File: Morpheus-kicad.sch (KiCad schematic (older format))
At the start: 60 parts, among them J1 Conn_02x03_Odd_Even, J2 Conn_02x03_Odd_Even, J3 Conn_02x03_Odd_Even, J4 Conn_02x03_Odd_Even, J5 Conn_02x05_Counter_Clockwise, J6 Conn_01x05, Q1 IRLZ44N, Q2 IRLB3034PBF, Q3 IRLZ44N, U1 Pololu Driver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

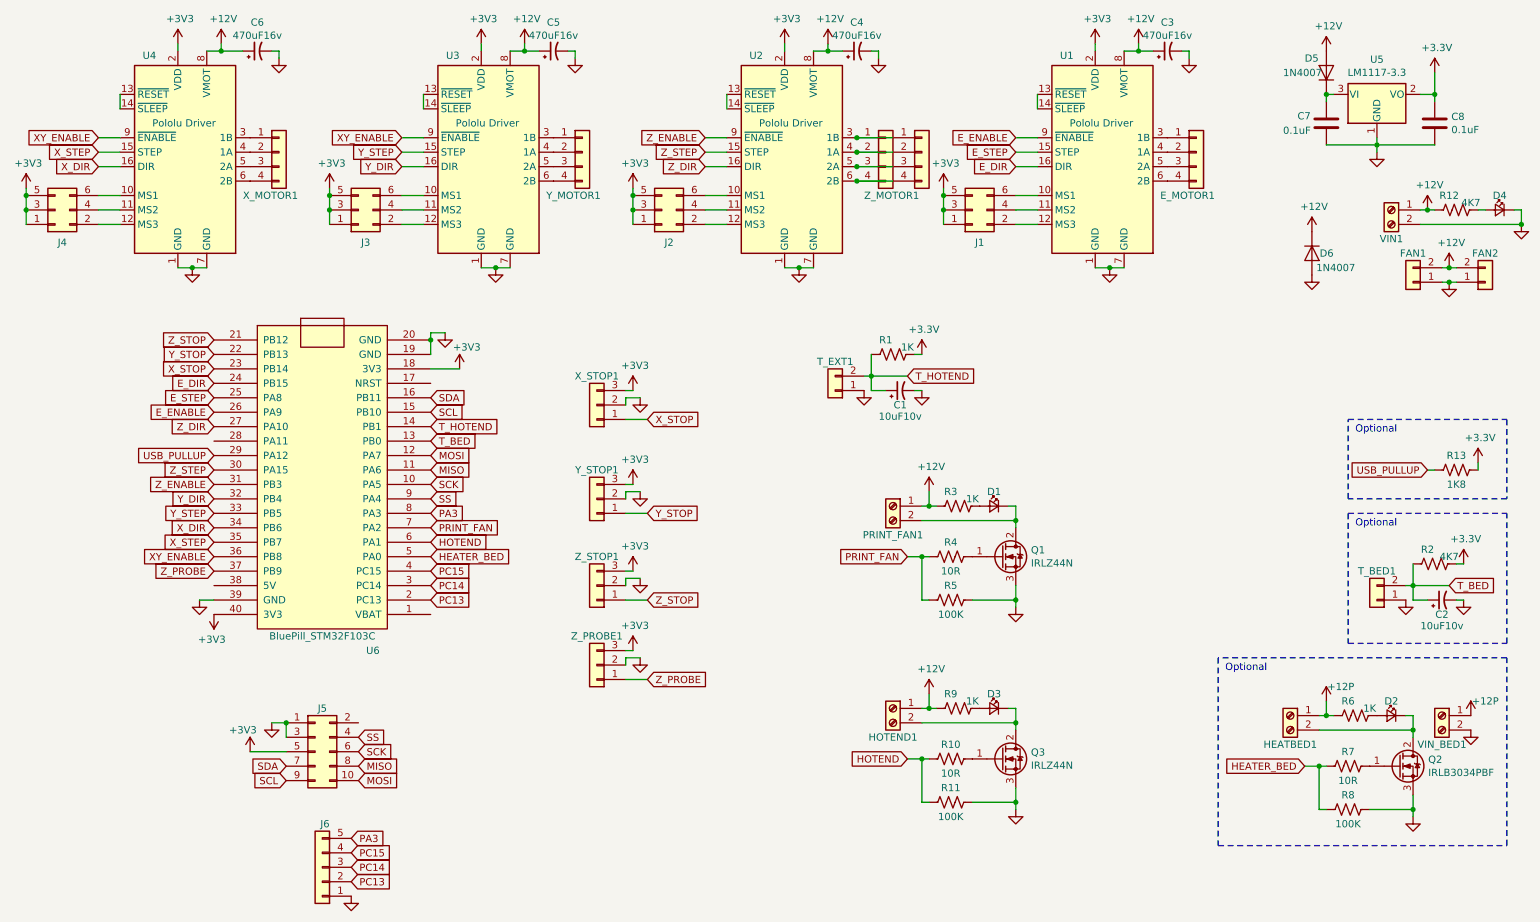
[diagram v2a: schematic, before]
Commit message: Modified headers and added teardrops
Re-organized J5 and J6 headers, and added teardrops on all pads, which helps a lot with home etching.
Also, after seeing some people who needed an external USB port, I added a small header to take out the USB data lines without changing the whole board.
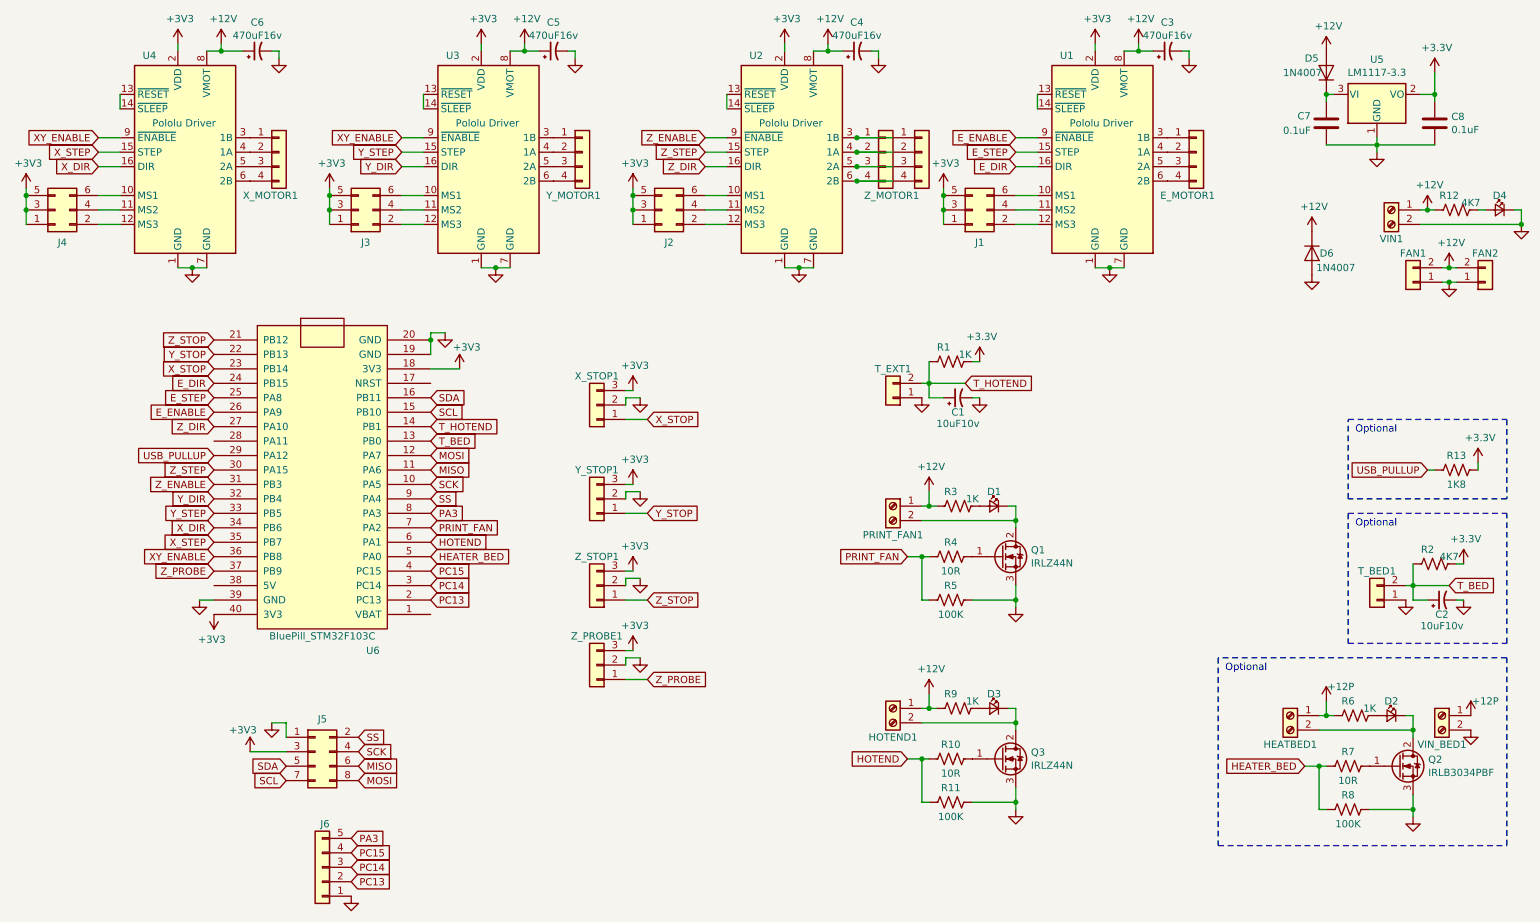
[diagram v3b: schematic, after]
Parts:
- removed J5: Conn_02x05_Counter_Clockwise, Connector_PinHeader_2.54mm:PinHeader_2x05_P2.54mm_Vertical, symbol Connector_Generic:Conn_02x05_Odd_Even
- added J5: Conn_02x04_Odd_Even, Connector_PinHeader_2.54mm:PinHeader_2x04_P2.54mm_Vertical, symbol Connector_Generic:Conn_02x04_Odd_Even
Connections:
- net +3V3: now also J5.3 (Pin_3)
- net GND: now also J5.1 (Pin_1)
- net MISO: now also J5.6 (Pin_6)
- net MOSI: now also J5.8 (Pin_8)
- net SCK: now also J5.4 (Pin_4)
- net SCL: now also J5.7 (Pin_7)
- net SDA: now also J5.5 (Pin_5)
- net SS: now also J5.2 (Pin_2)
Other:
- moved on the sheet: C1, R1, T_EXT1
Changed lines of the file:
@@
 EESchema Schematic File Version 4
-LIBS:Morpheus-kicad-cache
 EELAYER 30 0
 EELAYER END
@@
 Title "MORPHEUS Board by SPON!"
 Date ""
-Rev "0.6"
+Rev "0.9"
 Comp "Released under GPLv3"
 Comment1 ""
@@
 HEATER_BED
 $Comp
-L Connector_Generic:Conn_02x05_Odd_Even J5
-U 1 1 5BEE08E8
-P 2600 5650
-F 0 "J5" H 2650 5950 50  0000 C CNN
-F 1 "Conn_02x05_Counter_Clockwise" H 2650 5976 50  0001 C CNN
-F 2 "Connector_PinHeader_2.54mm:PinHeader_2x05_P2.54mm_Vertical" H 2600 5650 50  0001 C CNN
-F 3 "~" H 2600 5650 50  0001 C CNN
-	1    2600 5650
-	1    0    0    -1
-$EndComp
-$Comp
 L power:GND #PWR0128
 U 1 1 5BEE0B79
@@
 Wire Wire Line
 	2400 5450 2300 5450
-Connection ~ 2400 5450
 Wire Wire Line
 	2150 5650 2400 5650
@@
 L power:GND #PWR0136
 U 1 1 5BF0B443
-P 6400 3150
-F 0 "#PWR0136" H 6400 2900 50  0001 C CNN
-F 1 "GND" H 6405 2977 50  0001 C CNN
-F 2 "" H 6400 3150 50  0001 C CNN
-F 3 "" H 6400 3150 50  0001 C CNN
-	1    6400 3150
+P 6800 3200
+F 0 "#PWR0136" H 6800 2950 50  0001 C CNN
+F 1 "GND" H 6805 3027 50  0001 C CNN
+F 2 "" H 6800 3200 50  0001 C CNN
+F 3 "" H 6800 3200 50  0001 C CNN
+	1    6800 3200
 	1    0    0    -1
 $EndComp
@@
 L Device:R_US R1
 U 1 1 5BF160F7
-P 6600 2900
-F 0 "R1" V 6500 2850 50  0000 C CNN
-F 1 "1K" V 6550 3000 50  0000 C CNN
-F 2 "Resistor_THT:R_Axial_DIN0207_L6.3mm_D2.5mm_P7.62mm_Horizontal" V 6640 2890 50  0001 C CNN
-F 3 "~" H 6600 2900 50  0001 C CNN
-	1    6600 2900
+P 7000 2950
+F 0 "R1" V 6900 2900 50  0000 C CNN
+F 1 "1K" V 6950 3050 50  0000 C CNN
+F 2 "Resistor_THT:R_Axial_DIN0207_L6.3mm_D2.5mm_P7.62mm_Horizontal" V 7040 2940 50  0001 C CNN
+F 3 "~" H 7000 2950 50  0001 C CNN
+	1    7000 2950
 	0    1    1    0
 $EndComp
-Text GLabel 6700 3050 2    50   Input ~ 0
+Text GLabel 7100 3100 2    50   Input ~ 0
 T_HOTEND
 $Comp
 L Device:CP1_Small C1
 U 1 1 5BF1E9D4
-P 6650 3150
-F 0 "C1" V 6550 3150 50  0000 C CNN
-F 1 "10uF10v" V 6500 3150 50  0000 C BNN
-F 2 "Capacitor_THT:CP_Radial_D5.0mm_P2.00mm" H 6650 3150 50  0001 C CNN
-F 3 "~" H 6650 3150 50  0001 C CNN
-	1    6650 3150
+P 7050 3200
+F 0 "C1" V 6950 3200 50  0000 C CNN
+F 1 "10uF10v" V 6900 3200 50  0000 C BNN
+F 2 "Capacitor_THT:CP_Radial_D5.0mm_P2.00mm" H 7050 3200 50  0001 C CNN
+F 3 "~" H 7050 3200 50  0001 C CNN
+	1    7050 3200
 	0    -1   -1   0
 $EndComp
 Wire Wire Line
-	6450 2900 6450 3050
-Wire Wire Line
-	6450 3050 6700 3050
-Wire Wire Line
-	6550 3150 6450 3150
-Wire Wire Line
-	6450 3150 6450 3050
-Connection ~ 6450 3050
-Wire Wire Line
-	6400 3050 6450 3050
-Wire Wire Line
-	6800 2900 6750 2900
+	6850 2950 6850 3100
+Wire Wire Line
+	6850 3100 7100 3100
+Wire Wire Line
+	6950 3200 6850 3200
+Wire Wire Line
+	6850 3200 6850 3100
+Connection ~ 6850 3100
+Wire Wire Line
+	6800 3100 6850 3100
+Wire Wire Line
+	7200 2950 7150 2950
 $Comp
 L Connector_Generic:Conn_01x02 T_EXT1
 U 1 1 5BF339C9
-P 6200 3150
-F 0 "T_EXT1" H 6200 2950 50  0000 C CNN
-F 1 "T_EXT" H 6120 2916 50  0001 C CNN
-F 2 "Connector_PinHeader_2.54mm:PinHeader_1x02_P2.54mm_Vertical" H 6200 3150 50  0001 C CNN
-F 3 "~" H 6200 3150 50  0001 C CNN
-	1    6200 3150
+P 6600 3200
+F 0 "T_EXT1" H 6600 3000 50  0000 C CNN
+F 1 "T_EXT" H 6520 2966 50  0001 C CNN
+F 2 "Connector_PinHeader_2.54mm:PinHeader_1x02_P2.54mm_Vertical" H 6600 3200 50  0001 C CNN
+F 3 "~" H 6600 3200 50  0001 C CNN
+	1    6600 3200
 	-1   0    0    1
 $EndComp
@@
 L power:GND #PWR0141
 U 1 1 5BF4C079
-P 6800 3150
-F 0 "#PWR0141" H 6800 2900 50  0001 C CNN
-F 1 "GND" H 6805 2977 50  0001 C CNN
-F 2 "" H 6800 3150 50  0001 C CNN
-F 3 "" H 6800 3150 50  0001 C CNN
-	1    6800 3150
+P 7200 3200
+F 0 "#PWR0141" H 7200 2950 50  0001 C CNN
+F 1 "GND" H 7205 3027 50  0001 C CNN
+F 2 "" H 7200 3200 50  0001 C CNN
+F 3 "" H 7200 3200 50  0001 C CNN
+	1    7200 3200
 	1    0    0    -1
 $EndComp
@@
 	10550 4600 10500 4600
 Wire Wire Line
-	6800 3150 6750 3150
+	7200 3200 7150 3200
 $Comp
 L Connector:Screw_Terminal_01x02 HEATBED1
@@
 L power:+3.3V #PWR0139
 U 1 1 5BECA72A
-P 6800 2900
-F 0 "#PWR0139" H 6800 2750 50  0001 C CNN
-F 1 "+3.3V" H 6815 3073 50  0000 C CNN
-F 2 "" H 6800 2900 50  0001 C CNN
-F 3 "" H 6800 2900 50  0001 C CNN
-	1    6800 2900
+P 7200 2950
+F 0 "#PWR0139" H 7200 2800 50  0001 C CNN
+F 1 "+3.3V" H 7215 3123 50  0000 C CNN
+F 2 "" H 7200 2950 50  0001 C CNN
+F 3 "" H 7200 2950 50  0001 C CNN
+	1    7200 2950
 	1    0    0    -1
 $EndComp
@@
 	1    0    0    -1
 $EndComp
+$Comp
+L Connector_Generic:Conn_02x04_Odd_Even J5
+U 1 1 5EBD8E99
+P 2600 5650
+F 0 "J5" H 2650 5876 50  0000 C CNN
+F 1 "Conn_02x04_Odd_Even" H 2650 5877 50  0001 C CNN
+F 2 "Connector_PinHeader_2.54mm:PinHeader_2x04_P2.54mm_Vertical" H 2600 5650 50  0001 C CNN
+F 3 "~" H 2600 5650 50  0001 C CNN
+	1    2600 5650
+	1    0    0    -1
+$EndComp
